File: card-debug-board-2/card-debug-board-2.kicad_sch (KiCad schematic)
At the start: 28 parts, among them J1 2-1734592-0, J2 Conn_01x05, J5 0676430910, J6 629105150521, SW1 PCM13SMTR, SW2 B3F-1000, SW3 CFS-0103TB, SW4 CFS-0103TB, U1 MIC5205-3.3YM5

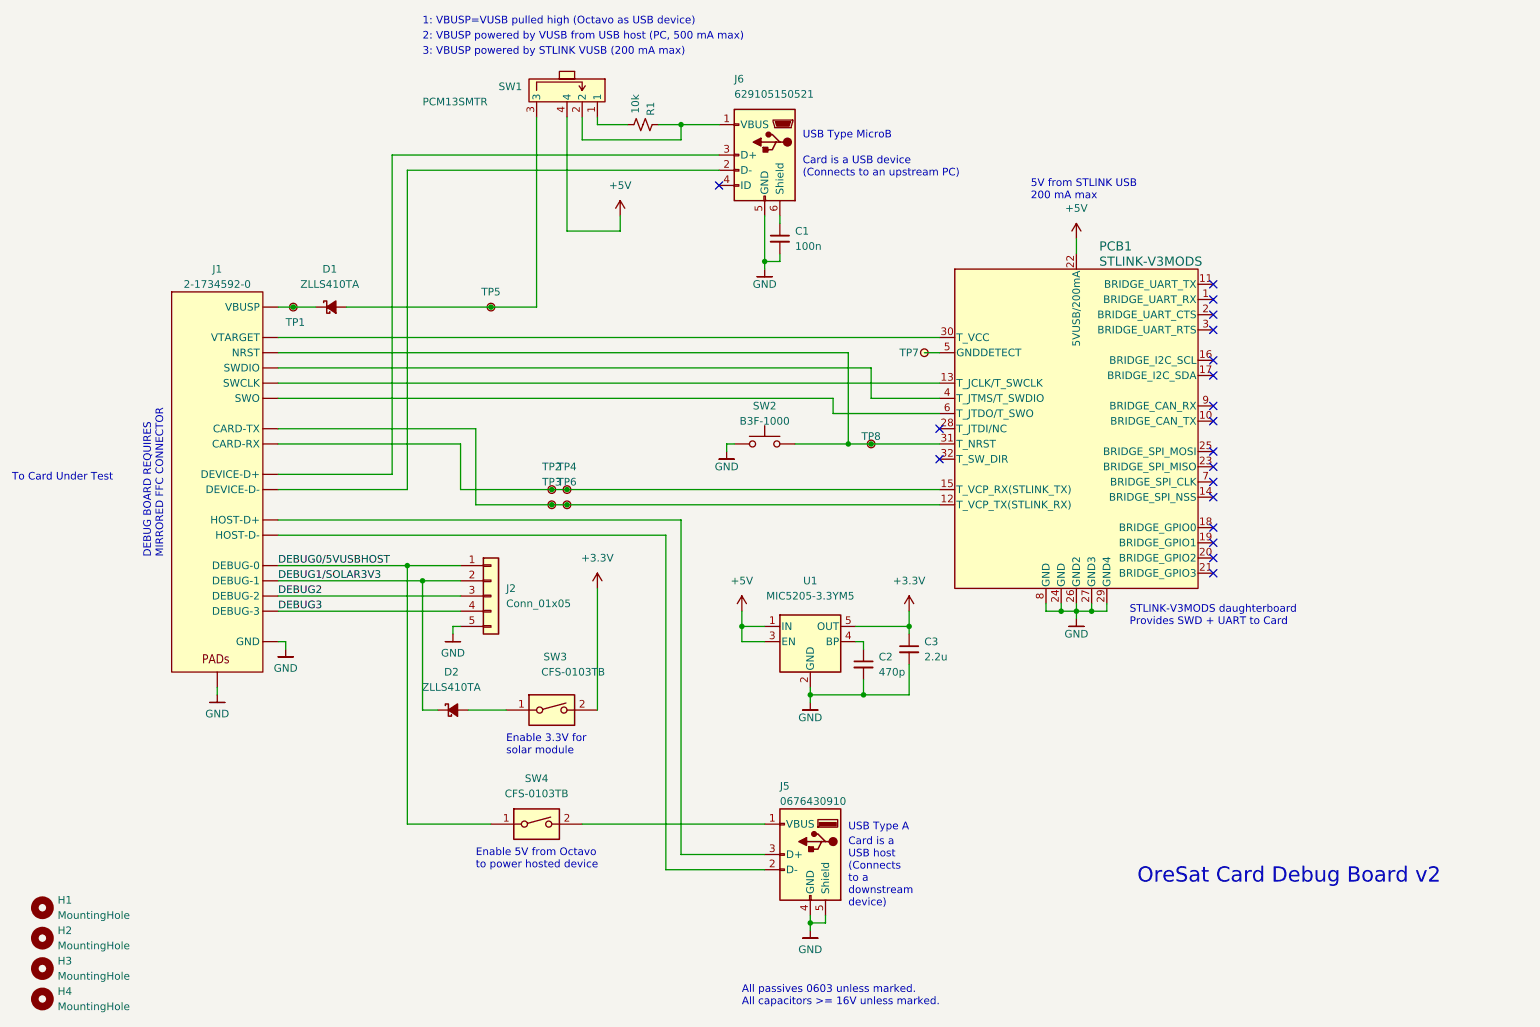
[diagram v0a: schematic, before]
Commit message: Completed rough draft layout of Card Debug Board v2.
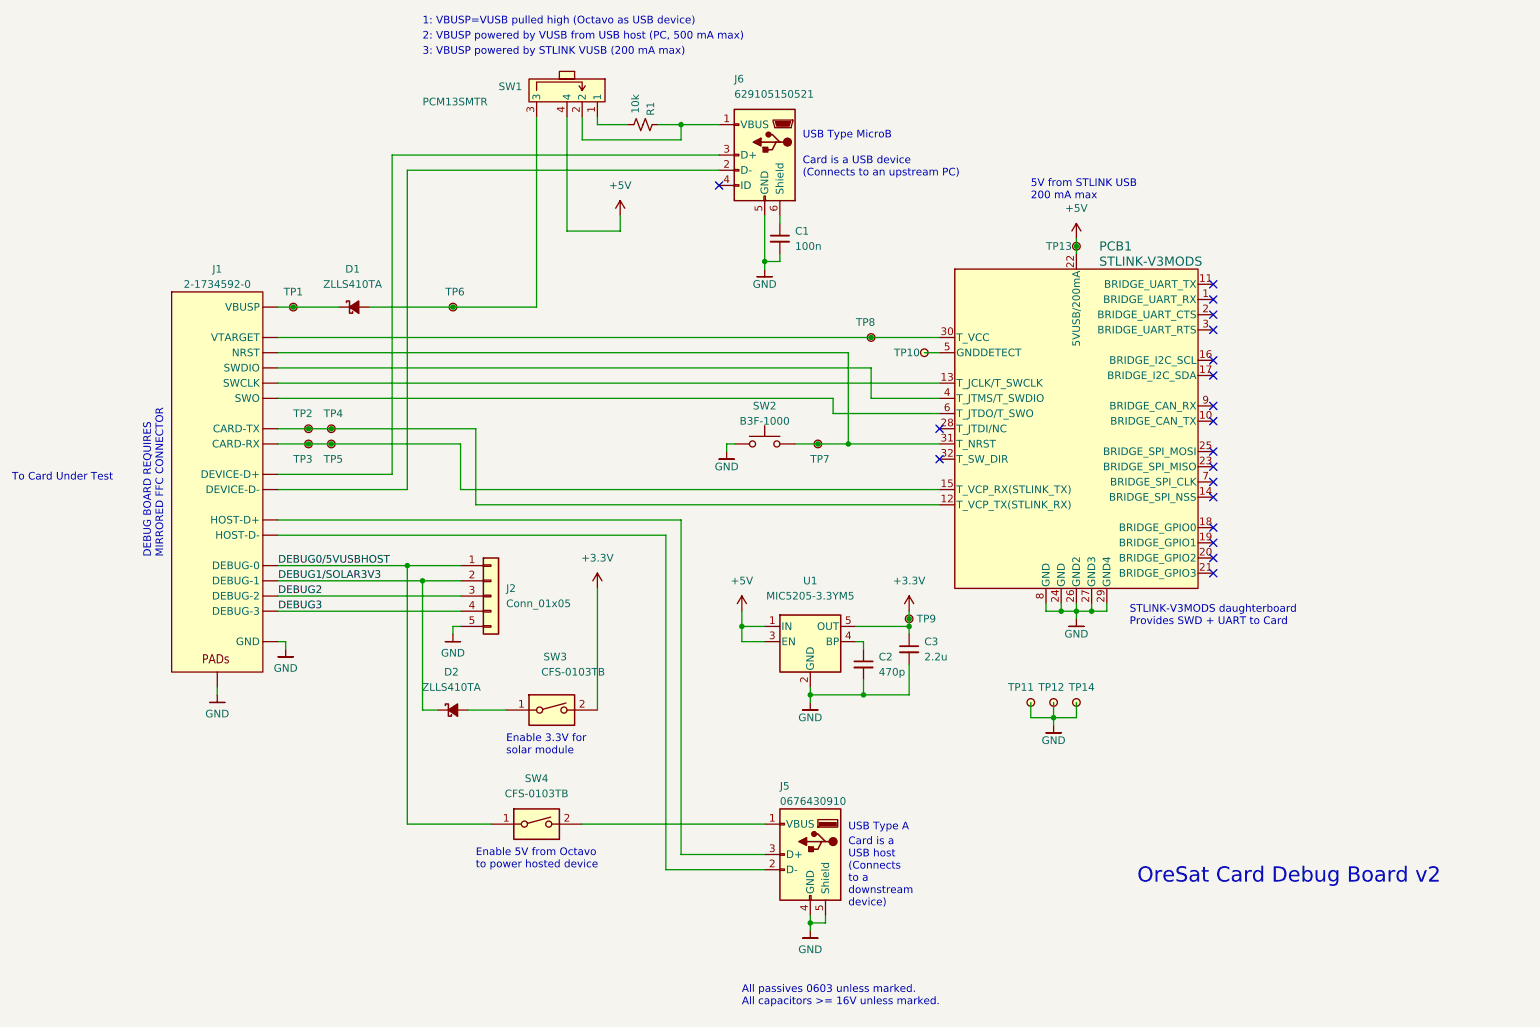
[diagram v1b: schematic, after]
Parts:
- removed H1, H2, H3, H4: MountingHole, MountingHole:MountingHole_3mm, symbol Mechanical:MountingHole
- added TP10, TP11, TP12, TP13, TP14, TP9: TestPoint-MinTH, oresat-misc:TestPoint-MinTH, symbol oresat-misc:TestPoint-MinTH
- D1, D2: Manufacturer Diodes Inc -> (none)
- J1: Manufacturer TE -> (none)
- J5: Manufacturer Molex -> (none)
- J6: Manufacturer Wurth -> (none)
- PCB1: Manufacturer ST Microelectronics -> (none)
- SW1: Manufacturer C&K -> (none)
- SW2: Manufacturer Omron -> (none)
- SW3, SW4: Manufacturer Nidec Copal -> (none)
- TP1, TP2, TP3, TP4, TP5, TP6, TP7, TP8: now left out of the parts list
- U1: Manufacturer Microchip -> (none)
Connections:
- net +3.3V: now also TP9.1
- net +5V: now also TP13.1
- net GND: now also TP11.1, TP12.1, TP14.1
- net at J1.10 (NRST), PCB1.31 (T_NRST), SW2.2: now also TP7.1; no longer TP8.1
- net at J1.13 (CARD-TX), PCB1.12 (T_VCP_TX(STLINK_RX)): now also TP2.1, TP4.1; no longer TP3.1, TP6.1
- net at D1.2 (A), SW1.3: now also TP6.1; no longer TP5.1
- net at J1.12 (CARD-RX), PCB1.15 (T_VCP_RX(STLINK_TX)): now also TP3.1, TP5.1; no longer TP2.1, TP4.1
- net at J1.11 (VTARGET), PCB1.30 (T_VCC): now also TP8.1
- net at PCB1.5 (GNDDETECT): now also TP10.1; no longer TP7.1
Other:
- moved on the sheet: D1

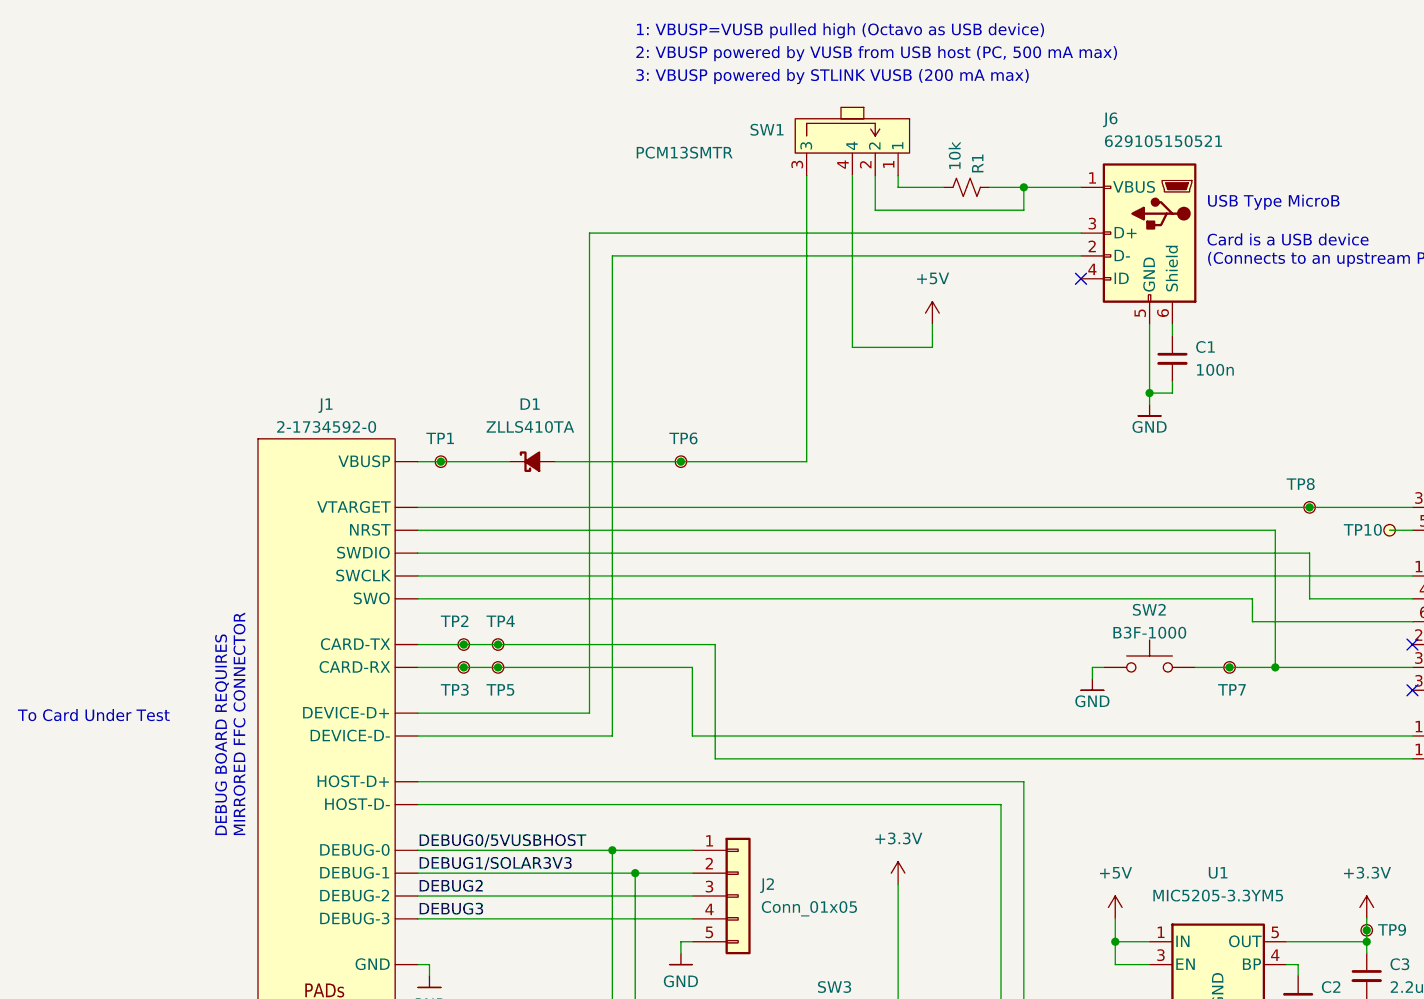
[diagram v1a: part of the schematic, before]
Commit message: Polish on the schematic and layout, including MFR/MPN additions, datasheet links, ground stitching, better text descriptions, etc.
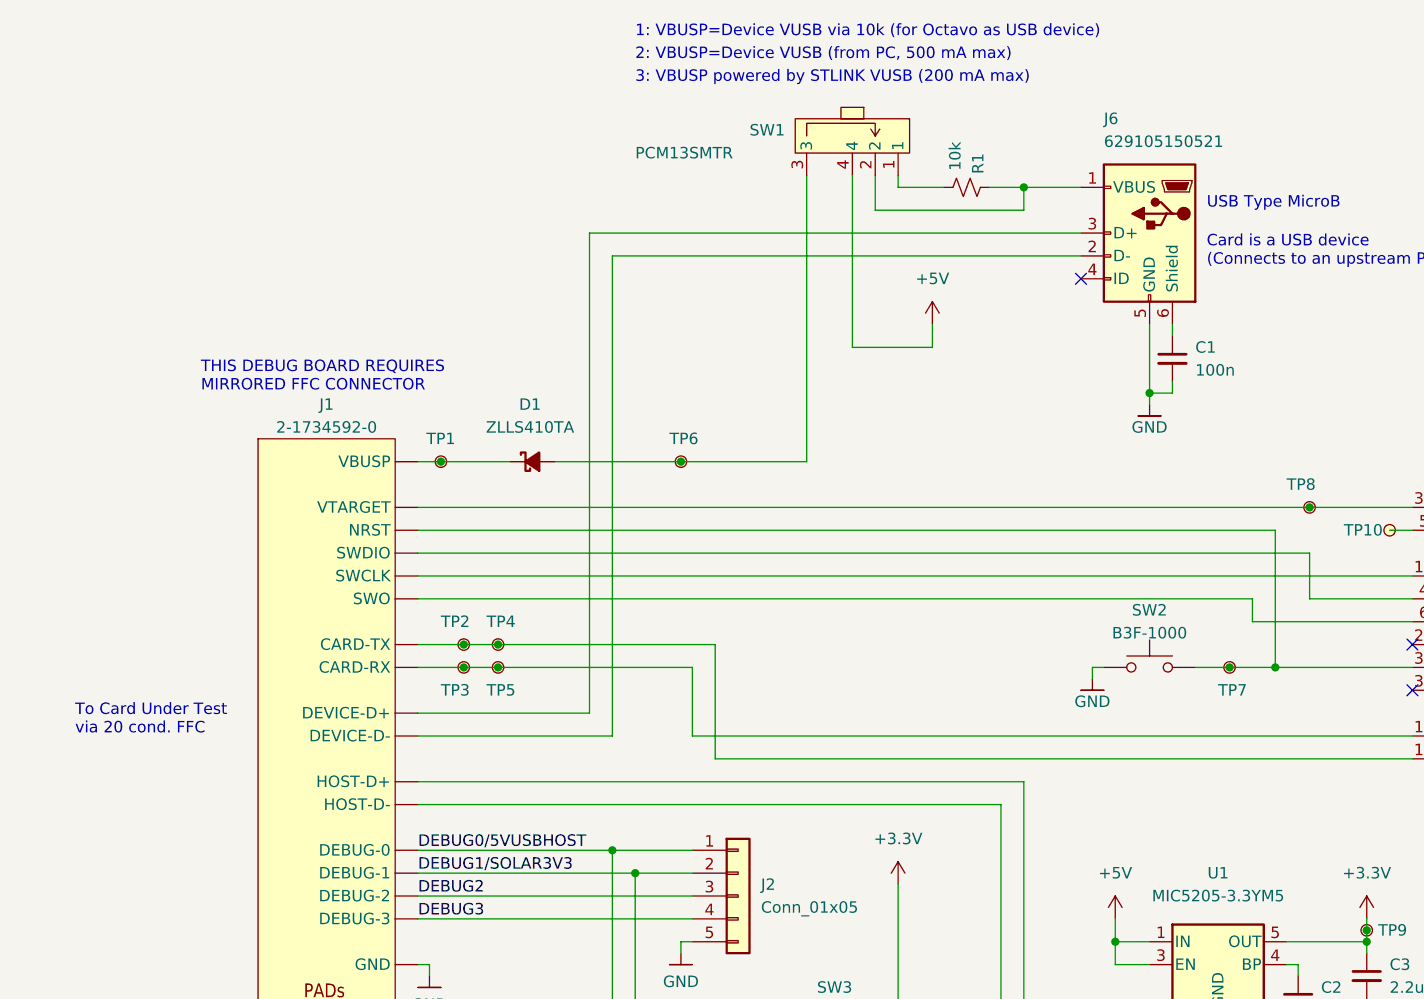
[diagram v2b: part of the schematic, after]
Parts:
- D1: MFR (none) -> ZLLS410TA; MPN (none) -> Diodes Inc
- D2: MFR (none) -> Diodes Inc; MPN (none) -> ZLLS410TA
- J1: MFR (none) -> TE Connectivity; MPN (none) -> 2-1734592-0
- J5: MFR (none) -> Molex; MPN (none) -> 0676430910
- J6: MFR (none) -> Würth Elektronik; MPN (none) -> 629105150521
- PCB1: MFR (none) -> ST Microelectronics; MPN (none) -> STLINK-V3MODS
- SW1: MFR (none) -> C&K; MPN (none) -> PCM13SMTR
- SW2: MFR (none) -> B3F-1000; MPN (none) -> Omron Electronics
- SW3, SW4: MFR (none) -> Nidec Copal Electronics; MPN (none) -> CFS-0103TB
- U1: MFR (none) -> Microchip Technology; MPN (none) -> MIC5205-3.3YM5-TR
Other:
- note added: "1: VBUSP=Device VUSB via 10k (for Octavo as USB device)"
- note added: "2: VBUSP=Device VUSB (from PC, 500 mA max)"
- note added: "THIS DEBUG BOARD REQUIRES MIRRORED FFC CONNECTOR"
- note added: "To Card Under Test via 20 cond. FFC"
- note removed: "1: VBUSP=VUSB pulled high (Octavo as USB device)"
- note removed: "2: VBUSP powered by VUSB from USB host (PC, 500 mA max)"
- note removed: "DEBUG BOARD REQUIRES MIRRORED FFC CONNECTOR"
- note removed: "To Card Under Test"
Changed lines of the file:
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@@
     (effects (font (size 1.27 1.27)) (justify left bottom))
   )
-  (text "2: VBUSP powered by VUSB from USB host (PC, 500 mA max)"
-    (at 82.55 34.29 0)
+  (text "2: VBUSP=Device VUSB (from PC, 500 mA max)" (at 82.55 34.29 0)
     (effects (font (size 1.27 1.27)) (justify left bottom))
   )
@@
     (effects (font (size 1.27 1.27)) (justify left bottom))
   )
-  (text "To Card Under Test" (at 13.97 107.95 0)
+  (text "To Card Under Test\nvia 20 cond. FFC" (at 20.32 109.22 0)
     (effects (font (size 1.27 1.27)) (justify left bottom))
   )
@@
     (effects (font (size 1.27 1.27)) (justify left bottom))
   )
-  (text "DEBUG BOARD REQUIRES\nMIRRORED FFC CONNECTOR" (at 39.37 120.65 90)
+  (text "THIS DEBUG BOARD REQUIRES\nMIRRORED FFC CONNECTOR" (at 34.29 71.12 0)
     (effects (font (size 1.27 1.27)) (justify left bottom))
   )
@@
     (effects (font (size 1.27 1.27)) (justify left bottom))
   )
-  (text "1: VBUSP=VUSB pulled high (Octavo as USB device)" (at 82.55 31.75 0)
+  (text "1: VBUSP=Device VUSB via 10k (for Octavo as USB device)"
+    (at 82.55 31.75 0)
     (effects (font (size 1.27 1.27)) (justify left bottom))
   )
@@
       (effects (font (size 1.27 1.27)) hide)
     )
-    (property "Datasheet" "~" (id 3) (at 139.7 96.52 0)
+    (property "Datasheet" "https://omronfs.omron.com/en_US/ecb/products/pdf/en-b3f.pdf" (id 3) (at 139.7 96.52 0)
+      (effects (font (size 1.27 1.27)) hide)
+    )
+    (property "MPN" "Omron Electronics" (id 4) (at 139.7 101.6 0)
+      (effects (font (size 1.27 1.27)) hide)
+    )
+    (property "MFR" "B3F-1000" (id 5) (at 139.7 101.6 0)
       (effects (font (size 1.27 1.27)) hide)
     )
@@
       (effects (font (size 1.27 1.27)) hide)
     )
-    (property "Datasheet" "~" (id 3) (at 71.12 78.74 90)
+    (property "Datasheet" "https://www.diodes.com/assets/Datasheets/ZLLS410.pdf" (id 3) (at 71.12 78.74 90)
+      (effects (font (size 1.27 1.27)) hide)
+    )
+    (property "MPN" "Diodes Inc" (id 4) (at 71.12 78.74 0)
+      (effects (font (size 1.27 1.27)) hide)
+    )
+    (property "MFR" "ZLLS410TA" (id 5) (at 71.12 78.74 0)
       (effects (font (size 1.27 1.27)) hide)
     )
@@
       (effects (font (size 1.27 1.27)) hide)
     )
-    (property "Datasheet" "~" (id 3) (at 104.14 146.05 0)
+    (property "Datasheet" "https://www.nidec-copal-electronics.com/e/catalog/switch/cfs.pdf" (id 3) (at 104.14 146.05 0)
+      (effects (font (size 1.27 1.27)) hide)
+    )
+    (property "MFR" "Nidec Copal Electronics" (id 4) (at 104.14 146.05 0)
+      (effects (font (size 1.27 1.27)) hide)
+    )
+    (property "MPN" "CFS-0103TB" (id 5) (at 104.14 146.05 0)
       (effects (font (size 1.27 1.27)) hide)
     )
@@
       (effects (font (size 1.27 1.27)) hide)
     )
-    (property "Datasheet" "~" (id 3) (at 135.89 54.61 0)
+    (property "Datasheet" "https://www.we-online.com/katalog/datasheet/629105150521.pdf" (id 3) (at 135.89 54.61 0)
+      (effects (font (size 1.27 1.27)) hide)
+    )
+    (property "MFR" "Würth Elektronik" (id 4) (at 139.7 53.34 0)
+      (effects (font (size 1.27 1.27)) hide)
+    )
+    (property "MPN" "629105150521" (id 5) (at 139.7 53.34 0)
       (effects (font (size 1.27 1.27)) hide)
     )
@@
     (property "Datasheet" "https://www.st.com/resource/en/user_manual/um2502-stlinkv3mods-and-stlinkv3mini-debuggerprogrammer-tiny-probes-for-stm32-microcontrollers-stmicroelectronics.pdf" (id 3) (at 191.77 55.88 0)
       (effects (font (size 1.524 1.524)) hide)
+    )
+    (property "MFR" "ST Microelectronics" (id 4) (at 191.77 99.06 0)
+      (effects (font (size 1.27 1.27)) hide)
+    )
+    (property "MPN" "STLINK-V3MODS" (id 5) (at 191.77 99.06 0)
+      (effects (font (size 1.27 1.27)) hide)
     )
     (pin "1")
@@
       (effects (font (size 1.524 1.524)) hide)
     )
+    (property "MFR" "C&K" (id 4) (at 106.68 41.91 0)
+      (effects (font (size 1.27 1.27)) hide)
+    )
+    (property "MPN" "PCM13SMTR" (id 5) (at 106.68 41.91 0)
+      (effects (font (size 1.27 1.27)) hide)
+    )
     (pin "1")
     (pin "2")
@@
       (effects (font (size 1.27 1.27)) hide)
     )
-    (property "Datasheet" " ~" (id 3) (at 143.51 171.45 0)
+    (property "Datasheet" "https://www.molex.com/pdm_docs/sd/676430910_sd.pdf" (id 3) (at 143.51 171.45 0)
+      (effects (font (size 1.27 1.27)) hide)
+    )
+    (property "MFR" "Molex" (id 4) (at 147.32 170.18 0)
+      (effects (font (size 1.27 1.27)) hide)
+    )
+    (property "MPN" "0676430910" (id 5) (at 147.32 170.18 0)
       (effects (font (size 1.27 1.27)) hide)
     )
@@
       (effects (font (size 1.27 1.27)) hide)
     )
+    (property "MFR" "Microchip Technology" (id 4) (at 147.32 134.62 0)
+      (effects (font (size 1.27 1.27)) hide)
+    )
+    (property "MPN" "MIC5205-3.3YM5-TR" (id 5) (at 147.32 134.62 0)
+      (effects (font (size 1.27 1.27)) hide)
+    )
     (pin "1")
     (pin "2")
@@
       (effects (font (size 1.27 1.27)) hide)
     )
-    (property "Datasheet" "" (id 3) (at 48.26 97.79 0)
+    (property "Datasheet" "https://www.te.com/commerce/DocumentDelivery/DDEController?Action=srchrtrv&DocNm=1734592&DocType=Customer+Drawing&DocLang=English&DocFormat=pdf&PartCntxt=2-1734592-0" (id 3) (at 48.26 97.79 0)
+      (effects (font (size 1.27 1.27)) hide)
+    )
+    (property "MFR" "TE Connectivity" (id 4) (at 48.26 106.68 0)
+      (effects (font (size 1.27 1.27)) hide)
+    )
+    (property "MPN" "2-1734592-0" (id 5) (at 48.26 106.68 0)
       (effects (font (size 1.27 1.27)) hide)
     )
@@
       (effects (font (size 1.27 1.27)) hide)
     )
-    (property "Datasheet" "~" (id 3) (at 101.6 165.1 0)
+    (property "Datasheet" "https://www.nidec-copal-electronics.com/e/catalog/switch/cfs.pdf" (id 3) (at 101.6 165.1 0)
+      (effects (font (size 1.27 1.27)) hide)
+    )
+    (property "MFR" "Nidec Copal Electronics" (id 4) (at 101.6 165.1 0)
+      (effects (font (size 1.27 1.27)) hide)
+    )
+    (property "MPN" "CFS-0103TB" (id 5) (at 101.6 165.1 0)
       (effects (font (size 1.27 1.27)) hide)
     )
@@
       (effects (font (size 1.27 1.27)) hide)
     )
-    (property "Datasheet" "~" (id 3) (at 87.63 146.05 90)
-      (effects (font (size 1.27 1.27)) hide)
-    )
+    (property "Datasheet" "https://www.diodes.com/assets/Datasheets/ZLLS410.pdf" (id 3) (at 87.63 146.05 90)
+      (effects (font (size 1.27 1.27)) hide)
+    )
+    (property "MFR" "Diodes Inc" (id 4) (at 87.63 146.05 0)
+      (effects (font (size 1.27 1.27)) hide)
+    )
+    (property "MPN" "ZLLS410TA" (id 5) (at 87.63 146.05 0)
+      (effects (font (size 1.27 1.27)) hide)
+    )
